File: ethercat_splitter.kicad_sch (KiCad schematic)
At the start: 14 parts

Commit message: [update] Positionning v1
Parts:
- removed FID1, FID2, FID3: DNP Fiducial, Fiducial:Fiducial_1mm_Mask2mm, symbol Mechanical:Fiducial
- removed H1: PCB01145, symbol Library_Pollen:PCB
- removed H10, H11, H12, H13: MountingHole_Pad, MountingHole:MountingHole_3.2mm_M3, symbol Mechanical:MountingHole
- removed H2: Logo HF 2025, Library_Pollen:Logo_HF_2025, symbol Library_Pollen:Logo HF 2025
- removed H3: DNP Logo Pollen 2021, Library_Pollen:Logo_Pollen_2021_sq, symbol Library_Pollen:Logo Pollen 2021
- removed H4, H5, H6, H7: MountingHole_Pad, MountingHole:MountingHole_3.2mm_M3_ISO7380_Pad_TopBottom, symbol Mechanical:MountingHole_Pad
- added J10, J11, J12: PicoBlade 5, Connector_Molex:Molex_PicoBlade_53398-0571_1x05-1MP_P1.25mm_Vertical, symbol Connector_Generic_MountingPin:Conn_01x05_MountingPin
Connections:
- net GND: now also J10.1 (Pin_1), J10.MP (MountPin), J11.1 (Pin_1), J11.MP (MountPin), J12.1 (Pin_1), J12.MP (MountPin)
- new net: J10.4 (Pin_4), J12.2 (Pin_2)
- new net: J10.5 (Pin_5), J12.3 (Pin_3)
- new net: J11.2 (Pin_2), J12.4 (Pin_4)
- new net: J11.3 (Pin_3), J12.5 (Pin_5)
- new net: J10.2 (Pin_2), J11.4 (Pin_4)
- new net: J10.3 (Pin_3), J11.5 (Pin_5)
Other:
- removed sheet Dynamixel RS485
- removed sheet Dynamixel TTL
- removed sheet EtherCAT splitter
- removed sheet USB hub
- note added: "Left Shoulder"
- note added: "Neck"
- note added: "Right Shoulder"
- note added: "Rx+"
- note added: "Rx-"
- note added: "Tx+"
- note added: "Tx-"
- note removed: ""elec_maroilles" is USB 2.0 hub built with lockable USB connectors. It provides also Dynamixel TTL and Dynamixel RS485 converters and the associated connectors for Reachy 2's grippers and antennas."
- note removed: "A1"
- note removed: "ASE01146"
- note removed: "Cable-tie holes - Ø3mm"
- note removed: "Check"
- note removed: "Comments"
- note removed: "Date"
- note removed: "Designer"
- note removed: "EB"
- note removed: "Fiducials"
- note removed: "Initial drawing"
- note removed: "Mounting Holes M3"
- note removed: "Release"
- note removed: "SN"
- note removed: "xx/yy/2025"

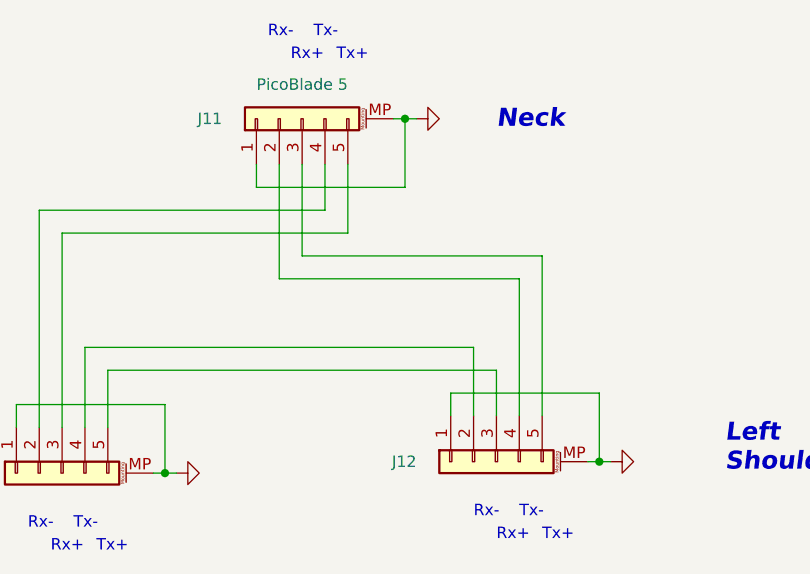
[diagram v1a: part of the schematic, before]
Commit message: [update] Better positionning.
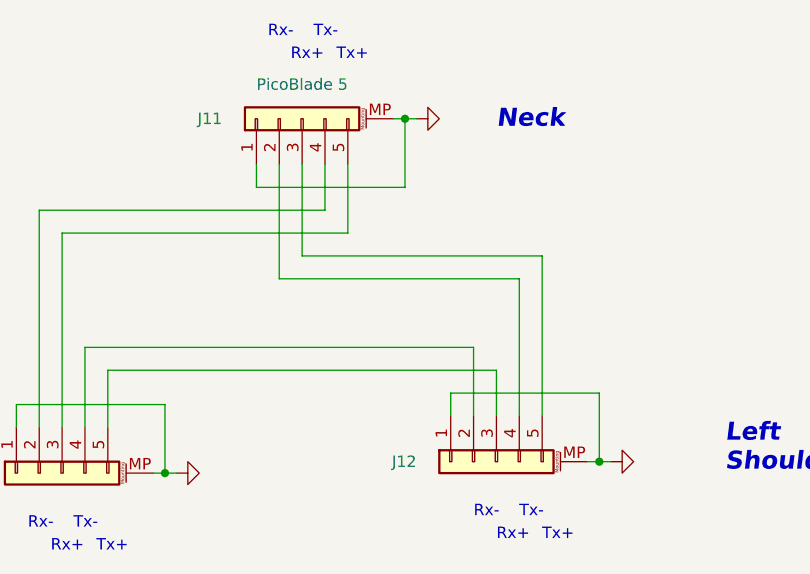
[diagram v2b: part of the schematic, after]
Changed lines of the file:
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@@
-	)
-	(symbol
-		(lib_id "power:GND")
-		(at 90.17 78.74 90)
-		(unit 1)
-		(exclude_from_sim no)
-		(in_bom yes)
-		(on_board yes)
-		(dnp no)
-		(fields_autoplaced yes)
-		(property "Reference" "#PWR072"
-			(at 96.52 78.74 0)
-			(effects
-				(font
-					(size 1.27 1.27)
-				)
-				(hide yes)
-			)
-		)
-		(property "Value" "GND"
-			(at 95.25 78.74 0)
-			(effects
-				(font
-					(size 1.27 1.27)
-				)
-				(hide yes)
-			)
-		)
-		(property "Footprint" ""
-			(at 90.17 78.74 0)
-			(effects
-				(font
-					(size 1.27 1.27)
-				)
-				(hide yes)
-			)
-		)
-		(property "Datasheet" ""
-			(at 90.17 78.74 0)
-			(effects
-				(font
-					(size 1.27 1.27)
-				)
-				(hide yes)
-			)
-		)
-		(property "Description" ""
-			(at 90.17 78.74 0)
-			(effects
-				(font
-					(size 1.27 1.27)
-				)
-			)
-		)
-		(pin "1"
-		)
-		(instances
-			(project "elec_maroilles"
-				(path "/bc05f5da-608c-4912-90e4-36b13d989976/04028f59-f620-48fc-9917-8d603b3905a4"
-					(reference "#PWR072")
-					(unit 1)
-				)
-			)
-		)
-	)
-	(symbol
-		(lib_id "power:GND")
-		(at 138.43 77.47 90)
-		(unit 1)
-		(exclude_from_sim no)
-		(in_bom yes)
-		(on_board yes)
-		(dnp no)
-		(fields_autoplaced yes)
-		(property "Reference" "#PWR074"
-			(at 144.78 77.47 0)
-			(effects
-				(font
-					(size 1.27 1.27)
-				)
-				(hide yes)
-			)
-		)
-		(property "Value" "GND"
-			(at 143.51 77.47 0)
-			(effects
-				(font
-					(size 1.27 1.27)
-				)
-				(hide yes)
-			)
-		)
-		(property "Footprint" ""
-			(at 138.43 77.47 0)
-			(effects
-				(font
-					(size 1.27 1.27)
-				)
-				(hide yes)
-			)
-		)
-		(property "Datasheet" ""
-			(at 138.43 77.47 0)
-			(effects
-				(font
-					(size 1.27 1.27)
-				)
-				(hide yes)
-			)
-		)
-		(property "Description" ""
-			(at 138.43 77.47 0)
-			(effects
-				(font
-					(size 1.27 1.27)
-				)
-			)
-		)
-		(pin "1"
-		)
-		(instances
-			(project "elec_maroilles"
-				(path "/bc05f5da-608c-4912-90e4-36b13d989976/04028f59-f620-48fc-9917-8d603b3905a4"
-					(reference "#PWR074")
-					(unit 1)
-				)
-			)
-		)
 	)
 	(symbol
@@
 		(lib_id "power:GND")
 		(at 116.84 39.37 90)
+		(mirror x)
 		(unit 1)
 		(exclude_from_sim no)
@@
 		(dnp no)
 		(fields_autoplaced yes)
-		(property "Reference" "#PWR073"
+		(property "Reference" "#PWR022"
 			(at 123.19 39.37 0)
 			(effects
@@
 			)
 		)
-		(property "Description" ""
+		(property "Description" "Power symbol creates a global label with name \"GND\" , ground"
 			(at 116.84 39.37 0)
 			(effects
@@
 					(size 1.27 1.27)
 				)
+				(hide yes)
 			)
 		)
@@
 			(project "elec_maroilles"
 				(path "/bc05f5da-608c-4912-90e4-36b13d989976/04028f59-f620-48fc-9917-8d603b3905a4"
-					(reference "#PWR073")
+					(reference "#PWR022")
+					(unit 1)
+				)
+			)
+		)
+	)
+	(symbol
+		(lib_id "power:GND")
+		(at 138.43 77.47 90)
+		(mirror x)
+		(unit 1)
+		(exclude_from_sim no)
+		(in_bom yes)
+		(on_board yes)
+		(dnp no)
+		(fields_autoplaced yes)
+		(property "Reference" "#PWR017"
+			(at 144.78 77.47 0)
+			(effects
+				(font
+					(size 1.27 1.27)
+				)
+				(hide yes)
+			)
+		)
+		(property "Value" "GND"
+			(at 143.51 77.47 0)
+			(effects
+				(font
+					(size 1.27 1.27)
+				)
+				(hide yes)
+			)
+		)
+		(property "Footprint" ""
+			(at 138.43 77.47 0)
+			(effects
+				(font
+					(size 1.27 1.27)
+				)
+				(hide yes)
+			)
+		)
+		(property "Datasheet" ""
+			(at 138.43 77.47 0)
+			(effects
+				(font
+					(size 1.27 1.27)
+				)
+				(hide yes)
+			)
+		)
+		(property "Description" "Power symbol creates a global label with name \"GND\" , ground"
+			(at 138.43 77.47 0)
+			(effects
+				(font
+					(size 1.27 1.27)
+				)
+				(hide yes)
+			)
+		)
+		(pin "1"
+		)
+		(instances
+			(project "elec_maroilles"
+				(path "/bc05f5da-608c-4912-90e4-36b13d989976/04028f59-f620-48fc-9917-8d603b3905a4"
+					(reference "#PWR017")
 					(unit 1)
 				)
@@
 					(unit 1)
 				)
+			)
+		)
+	)
+	(symbol
+		(lib_id "power:GND")
+		(at 90.17 78.74 90)
+		(mirror x)
+		(unit 1)
+		(exclude_from_sim no)
+		(in_bom yes)
+		(on_board yes)
+		(dnp no)
+		(fields_autoplaced yes)
+		(property "Reference" "#PWR018"
+			(at 96.52 78.74 0)
+			(effects
+				(font
+					(size 1.27 1.27)
+				)
+				(hide yes)
+			)
+		)
+		(property "Value" "GND"
+			(at 95.25 78.74 0)
+			(effects
+				(font
+					(size 1.27 1.27)
+				)
+				(hide yes)
+			)
+		)
+		(property "Footprint" ""
+			(at 90.17 78.74 0)
+			(effects
+				(font
+					(size 1.27 1.27)
+				)
+				(hide yes)
+			)
+		)
+		(property "Datasheet" ""
+			(at 90.17 78.74 0)
+			(effects
+				(font
+					(size 1.27 1.27)
+				)
+				(hide yes)
+			)
+		)
+		(property "Description" "Power symbol creates a global label with name \"GND\" , ground"
+			(at 90.17 78.74 0)
+			(effects
+				(font
+					(size 1.27 1.27)
+				)
+				(hide yes)
+			)
+		)
+		(pin "1"
+		)
+		(instances
+			(project "elec_maroilles"
+				(path "/bc05f5da-608c-4912-90e4-36b13d989976/04028f59-f620-48fc-9917-8d603b3905a4"
+					(reference "#PWR018")
+					(unit 1)
+				)
